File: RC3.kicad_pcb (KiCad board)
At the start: 2 copper layers, 84.8 x 91.4 mm, 62 parts, among them P1 CONN_2, P2 CONN_3, P3 CONN_3X2, P4 CONN_2, Q1 MOSFET_N, Q10 MOSFET_N, Q11 MOSFET_N, Q12 MOSFET_N, Q13 MOSFET_N, Q14 MOSFET_N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

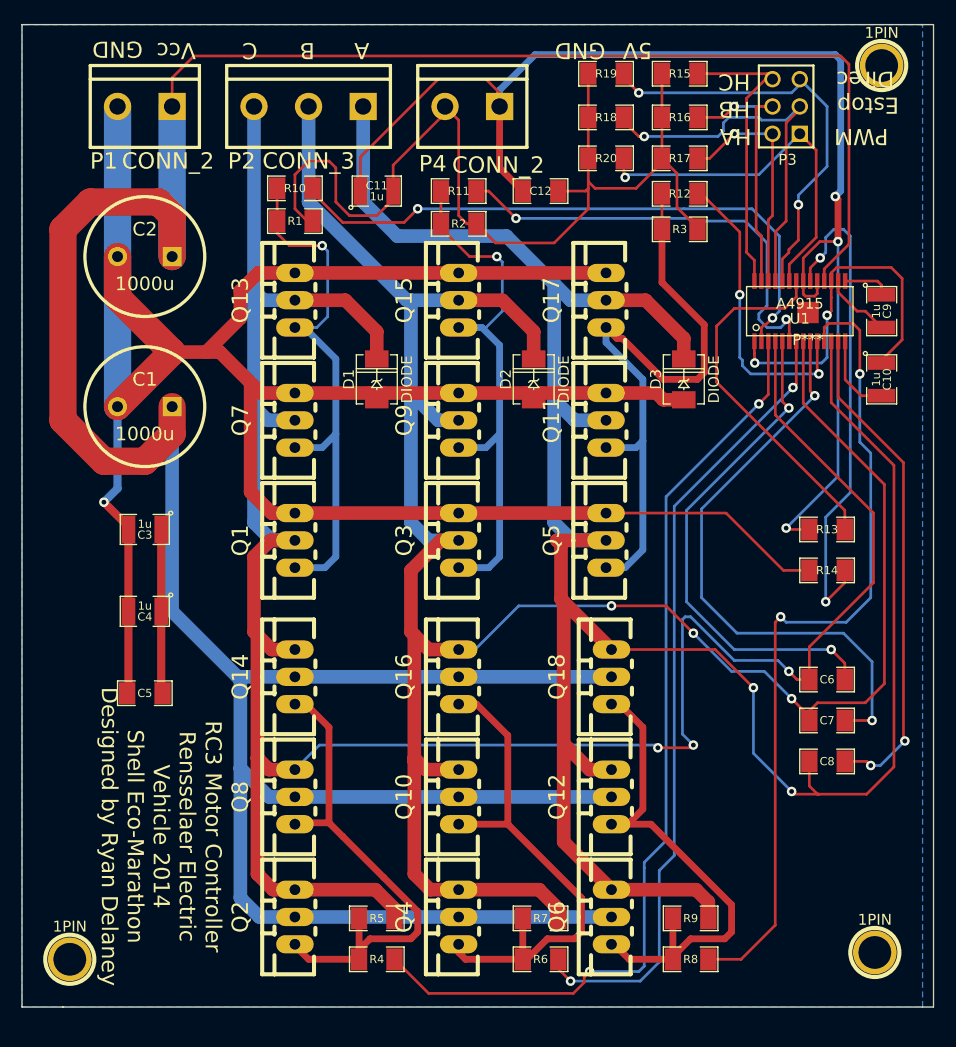
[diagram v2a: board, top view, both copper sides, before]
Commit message: Extended the keepout zone and added 4th hole
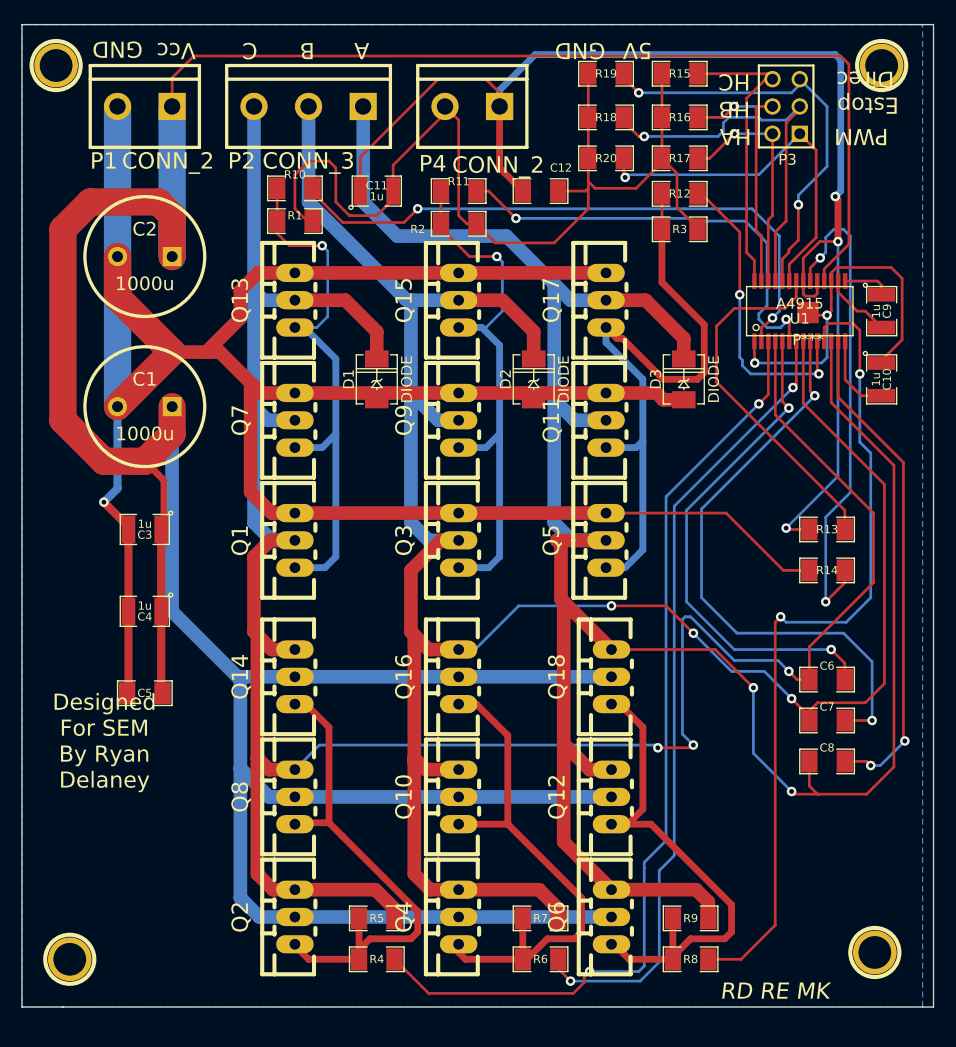
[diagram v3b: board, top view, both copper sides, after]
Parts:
- added ?: , 1pin, F.Cu at (145.4, 139.7)
- ? (x3): renamed from 1PIN; value P*** -> (none)
- P3: value CONN_3X2 -> (none)
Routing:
- net +48V: track 319.8 -> 327.0 mm
- net GND: track 359.8 -> 361.7 mm
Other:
- board text added: "Designed For SEM By Ryan Delaney"
- board text added: "RD RE MK"
- board text removed: "RC3 Motor Controller Rensselaer Electric Vehicle 2014 Shell Eco-Marathon Designed by Ryan Delaney"
- board text removed: "RD;SS;BL;AG;LCIII BP;KS;NR;JF;KW TD;JC;G;NT;ZA MD;SI;AL;VN;BL"
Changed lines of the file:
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@@
 (kicad_pcb (version 3) (host pcbnew "(2013-07-07 BZR 4022)-stable")
   (general
-    (links 133)
-    (no_connects 1)
-    (area 140.008286 135.839999 227.126001 227.380001)
+    (links 134)
+    (no_connects 0)
+    (area 142.189999 134.6175 227.126001 227.380001)
     (thickness 1.6)
     (drawings 23)
-    (tracks 627)
+    (tracks 632)
     (zones 0)
-    (modules 62)
+    (modules 63)
     (nets 33)
   )
@@
   )
   (setup
-    (last_trace_width 0.254)
+    (last_trace_width 0.635)
     (user_trace_width 0.635)
     (user_trace_width 0.762)
@@
     (at 167.64 154.178 180)
     (attr smd)
-    (fp_text reference R1 (at 0 0 180) (layer F.SilkS)
+    (fp_text reference R1 (at 0 0.508 180) (layer F.SilkS)
       (effects (font (size 0.762 0.762) (thickness 0.127)))
     )
-    (fp_text value 10K (at 0 0 180) (layer F.SilkS) hide
+    (fp_text value 10K (at -3.175 -0.127 270) (layer F.SilkS) hide
       (effects (font (size 0.762 0.762) (thickness 0.127)))
     )
@@
     (at 167.64 151.13)
     (attr smd)
-    (fp_text reference R10 (at 0 0) (layer F.SilkS)
+    (fp_text reference R10 (at 0 -1.27) (layer F.SilkS)
       (effects (font (size 0.762 0.762) (thickness 0.127)))
     )
-    (fp_text value 10K (at 0 0) (layer F.SilkS) hide
+    (fp_text value 10K (at 0 0.635 90) (layer F.SilkS) hide
       (effects (font (size 0.762 0.762) (thickness 0.127)))
     )
@@
     (at 217.17 196.85 180)
     (attr smd)
-    (fp_text reference C6 (at 0 0 180) (layer F.SilkS)
+    (fp_text reference C6 (at 0 1.27 180) (layer F.SilkS)
       (effects (font (size 0.762 0.762) (thickness 0.127)))
     )
-    (fp_text value 47n (at 0 0 180) (layer F.SilkS) hide
+    (fp_text value 47n (at 0 -0.635 270) (layer F.SilkS) hide
       (effects (font (size 0.762 0.762) (thickness 0.127)))
     )
@@
     (at 182.88 154.432 180)
     (attr smd)
-    (fp_text reference R2 (at 0 0 180) (layer F.SilkS)
+    (fp_text reference R2 (at 3.81 -0.508 180) (layer F.SilkS)
       (effects (font (size 0.762 0.762) (thickness 0.127)))
     )
-    (fp_text value 10K (at 0 0 180) (layer F.SilkS) hide
+    (fp_text value 10K (at 0 -0.508 270) (layer F.SilkS) hide
       (effects (font (size 0.762 0.762) (thickness 0.127)))
     )
@@
     (at 182.88 151.384)
     (attr smd)
-    (fp_text reference R11 (at 0 0) (layer F.SilkS)
+    (fp_text reference R11 (at 0 -0.889) (layer F.SilkS)
       (effects (font (size 0.762 0.762) (thickness 0.127)))
     )
-    (fp_text value 10K (at 0 0) (layer F.SilkS) hide
+    (fp_text value 10K (at 0 1.016 90) (layer F.SilkS) hide
       (effects (font (size 0.762 0.762) (thickness 0.127)))
     )
@@
     (at 217.17 204.47 180)
     (attr smd)
-    (fp_text reference C8 (at 0 0 180) (layer F.SilkS)
+    (fp_text reference C8 (at 0 1.27 180) (layer F.SilkS)
       (effects (font (size 0.762 0.762) (thickness 0.127)))
     )
-    (fp_text value 47n (at 0 0 180) (layer F.SilkS) hide
+    (fp_text value 47n (at 0 -0.635 270) (layer F.SilkS) hide
       (effects (font (size 0.762 0.762) (thickness 0.127)))
     )
@@
     (at 217.17 200.66 180)
     (attr smd)
-    (fp_text reference C7 (at 0 0 180) (layer F.SilkS)
+    (fp_text reference C7 (at 0 1.27 180) (layer F.SilkS)
       (effects (font (size 0.762 0.762) (thickness 0.127)))
     )
-    (fp_text value 47n (at 0 0 180) (layer F.SilkS) hide
+    (fp_text value 47n (at 0 -0.635 270) (layer F.SilkS) hide
       (effects (font (size 0.762 0.762) (thickness 0.127)))
     )
@@
       (effects (font (size 1.016 1.016) (thickness 0.2032)))
     )
-    (fp_text value CONN_3X2 (at 0 3.81 90) (layer F.SilkS) hide
+    (fp_text value "" (at 0 3.81 90) (layer F.SilkS) hide
       (effects (font (size 1.016 1.016) (thickness 0.2032)))
     )
@@
     (at 190.5 151.384)
     (attr smd)
-    (fp_text reference C12 (at 0 0) (layer F.SilkS)
+    (fp_text reference C12 (at 1.905 -2.159) (layer F.SilkS)
       (effects (font (size 0.762 0.762) (thickness 0.127)))
     )
-    (fp_text value 47n (at 0 0) (layer F.SilkS) hide
+    (fp_text value 47n (at 0 -0.254 90) (layer F.SilkS) hide
       (effects (font (size 0.762 0.762) (thickness 0.127)))
     )
@@
     (tags DEV)
     (path 1pin)
-    (fp_text reference 1PIN (at 0 -3.048) (layer F.SilkS)
+    (fp_text reference "" (at 0 -3.048) (layer F.SilkS)
       (effects (font (size 1.016 1.016) (thickness 0.254)))
     )
-    (fp_text value P*** (at 0 2.794) (layer F.SilkS) hide
+    (fp_text value "" (at 0 2.794) (layer F.SilkS) hide
       (effects (font (size 1.016 1.016) (thickness 0.254)))
     )
@@
     (tags DEV)
     (path 1pin)
-    (fp_text reference 1PIN (at 0 -3.048) (layer F.SilkS)
+    (fp_text reference "" (at 0 -3.048) (layer F.SilkS)
       (effects (font (size 1.016 1.016) (thickness 0.254)))
     )
-    (fp_text value P*** (at 0 2.794) (layer F.SilkS) hide
+    (fp_text value "" (at 0 2.794) (layer F.SilkS) hide
       (effects (font (size 1.016 1.016) (thickness 0.254)))
     )
@@
     (tags DEV)
     (path 1pin)
-    (fp_text reference 1PIN (at 0 -3.048) (layer F.SilkS)
+    (fp_text reference "" (at 0 -3.048) (layer F.SilkS)
+      (effects (font (size 1.016 1.016) (thickness 0.254)))
+    )
+    (fp_text value "" (at 0 2.794) (layer F.SilkS) hide
+      (effects (font (size 1.016 1.016) (thickness 0.254)))
+    )
+    (fp_circle (center 0 0) (end 0 -2.286) (layer F.SilkS) (width 0.381))
+    (pad 1 thru_hole circle (at 0 0) (size 4.064 4.064) (drill 3.048)
+      (layers *.Cu *.Mask F.SilkS)
+    )
+  )
+  (module 1pin (layer F.Cu)
+    (at 145.415 139.7)
+    (descr "module 1 pin (ou trou mecanique de percage)")
+    (tags DEV)
+    (path 1pin)
+    (fp_text reference "" (at 0 -3.048) (layer F.SilkS)
       (effects (font (size 1.016 1.016) (thickness 0.254)))
     )
-    (fp_text value P*** (at 0 2.794) (layer F.SilkS) hide
+    (fp_text value "" (at 0 2.794) (layer F.SilkS) hide
       (effects (font (size 1.016 1.016) (thickness 0.254)))
     )
@@
     )
   )
+  (gr_text "RD RE MK" (at 212.2932 225.8568) (layer F.SilkS)
+    (effects (font (size 1.5 1.5) (thickness 0.3) italic))
+  )
+  (gr_text "Designed\nFor SEM\nBy Ryan \nDelaney" (at 149.9108 202.5904) (layer F.SilkS)
+    (effects (font (size 1.5 1.5) (thickness 0.3)))
+  )
   (target plus (at 148.59 134.62) (size 0.005) (width 0.1) (layer Edge.Cuts))
   (gr_line (start 227.076 227.33) (end 226.06 227.33) (angle 90) (layer Edge.Cuts) (width 0.1))
   (gr_line (start 227.076 135.89) (end 227.076 227.33) (angle 90) (layer Edge.Cuts) (width 0.1))
   (gr_line (start 225.933 135.89) (end 227.076 135.89) (angle 90) (layer Edge.Cuts) (width 0.1))
-  (gr_text "RD;SS;BL;AG;LCIII\nBP;KS;NR;JF;KW\nTD;JC;G;NT;ZA\nMD;SI;AL;VN;BL" (at 215.519 214.757) (layer B.SilkS)
-    (effects (font (size 1.5 1.5) (thickness 0.3)) (justify mirror))
-  )
   (gr_text 5V (at 199.517 138.303 180) (layer F.SilkS)
     (effects (font (size 1.5 1.5) (thickness 0.3)))
@@
     (effects (font (size 1.5 1.5) (thickness 0.3)))
   )
-  (gr_text "RC3 Motor Controller\nRensselaer Electric \nVehicle 2014\nShell Eco-Marathon\nDesigned by Ryan Delaney" (at 155.194 211.455 270) (layer F.SilkS)
-    (effects (font (size 1.5 1.5) (thickness 0.3)))
-  )
   (gr_line (start 142.24 227.33) (end 146.05 227.33) (angle 90) (layer Edge.Cuts) (width 0.1))
   (gr_line (start 142.24 135.89) (end 142.24 227.33) (angle 90) (layer Edge.Cuts) (width 0.1))
   (gr_line (start 226.06 135.89) (end 142.24 135.89) (angle 90) (layer Edge.Cuts) (width 0.1))
   (gr_line (start 146.05 227.33) (end 226.06 227.33) (angle 90) (layer Edge.Cuts) (width 0.1))
+  (segment (start 155.448 182.626) (end 155.194 182.88) (width 0.635) (layer F.Cu) (net 1))
+  (segment (start 155.448 178.308) (end 155.448 182.626) (width 0.635) (layer F.Cu) (net 1))
+  (segment (start 153.67 176.53) (end 155.448 178.308) (width 0.635) (layer F.Cu) (net 1))
   (segment (start 156.21 157.48) (end 156.21 153.67) (width 2.54) (layer F.Cu) (net 1))
   (segment (start 156.21 173.99) (end 156.21 171.45) (width 2.54) (layer F.Cu) (net 1))
@@
   (segment (start 213.36 145.034) (end 213.36 154.178) (width 0.254) (layer F.Cu) (net 4))
   (segment (start 214.63 143.764) (end 213.36 145.034) (width 0.254) (layer F.Cu) (net 4))
+  (segment (start 217.17 162.941) (end 215.646 162.941) (width 0.254) (layer F.Cu) (net 5))
+  (segment (start 215.646 162.941) (end 215.392 162.687) (width 0.254) (layer F.Cu) (net 5))
   (segment (start 194.945 151.13) (end 194.945 153.035) (width 0.254) (layer F.Cu) (net 5))
   (segment (start 186.309 156.21) (end 184.531 154.432) (width 0.254) (layer F.Cu) (net 5))
@@
     (polygon
       (pts
-        (xy 204.47 224.79) (xy 158.75 224.79) (xy 159.385 156.845) (xy 203.835 156.845)
+        (xy 204.47 224.79) (xy 158.75 224.79) (xy 159.385 156.845) (xy 159.512 135.89) (xy 177.673 135.89)
+        (xy 177.8 155.956) (xy 203.835 156.845)
       )
     )
